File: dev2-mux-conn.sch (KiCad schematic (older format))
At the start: 8 parts, among them J28 Device 2, U11 MAX4533, U14 74LS32, U36 LTC1391, U37 LTC1391, U38 LTC1391, U7 TS12A44514

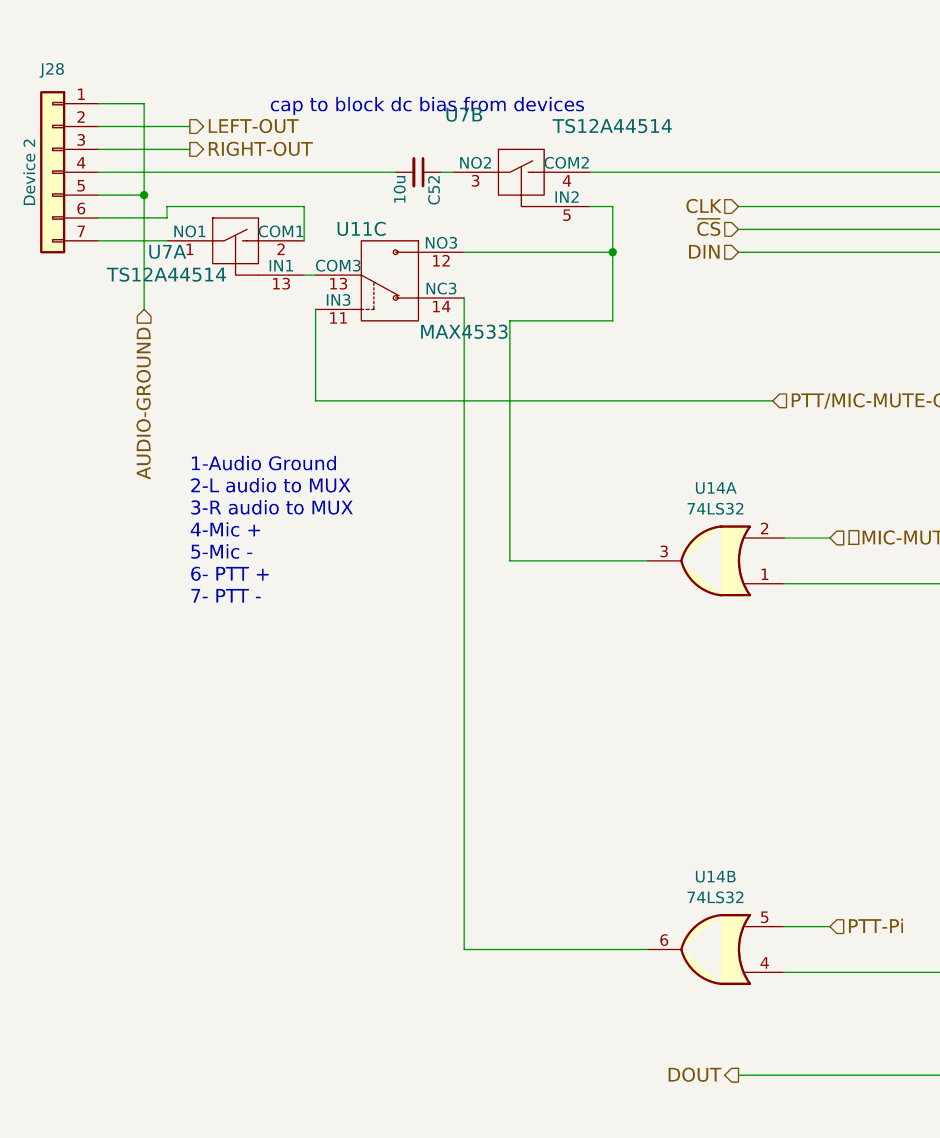
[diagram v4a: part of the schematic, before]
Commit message: Re arranging pins and component names
to make pcb layout saner
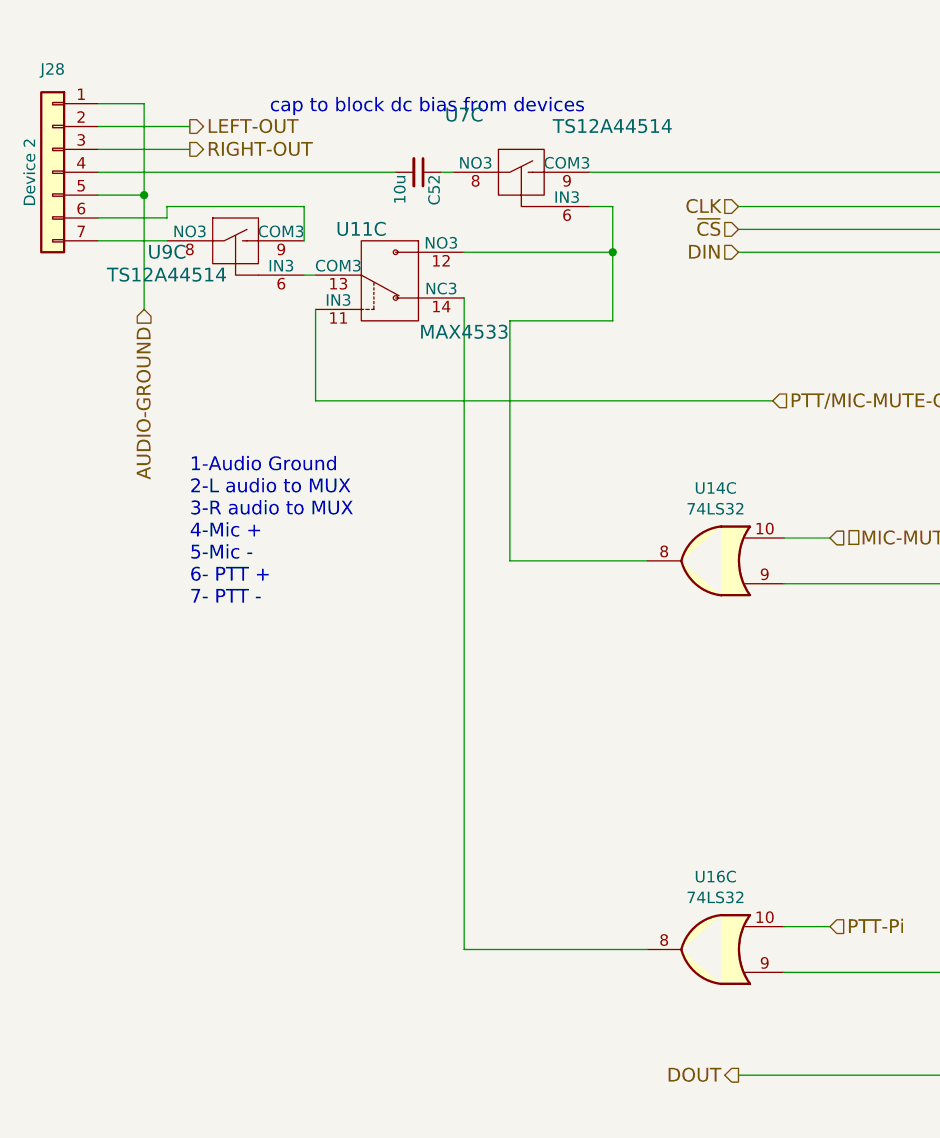
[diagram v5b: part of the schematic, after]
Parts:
- U14: Pricing (none) -> 0.00@0
- U16: renamed from U14; Pricing (none) -> 0.00@0
- renumbered U7 to U9
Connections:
- net MIC-MUTE-Pi: now also U14.10; no longer U14.2
- net PTT-Pi: now also U16.10; no longer U16.5
- net at J28.6 (Pin_6): now also U9.9 (COM3); no longer U9.2 (COM1)
- net at J28.7 (Pin_7): now also U9.8 (NO3); no longer U9.1 (NO1)
- net at C52.1: now also U7.8 (NO3); no longer U7.3 (NO2)
- net at U36.15 (D): now also U7.9 (COM3); no longer U7.4 (COM2)
- net at U11.13 (COM3): now also U9.6 (IN3); no longer U9.13 (IN1)
- net at U11.14 (NC3): now also U16.8; no longer U16.6
- net at U37.15 (D): now also U14.9; no longer U14.1
- net at U38.15 (D): now also U16.9; no longer U16.4
- new net: U11.12 (NO3), U14.8, U7.6 (IN3)
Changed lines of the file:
@@
 $Comp
 L TS12A44514 U?
-U 2 1 58EAA0E5
+U 3 1 58EAA0E5
 P 2950 1150
 AR Path="/58DEDA38/58EAA0E5" Ref="U?"  Part="1"
 AR Path="/58DEDA38/58E9E25B/58EAA0E5" Ref="U?"  Part="1"
-AR Path="/58DEDA38/58E9E991/58EAA0E5" Ref="U7"  Part="2"
+AR Path="/58DEDA38/58E9E991/58EAA0E5" Ref="U7"  Part="3"
 F 0 "U7" H 2700 1400 60  0000 C CNN
 F 1 "TS12A44514" H 3350 1350 60  0000 C CNN
@@
 F 7 "TSSOP14" H 3250 2350 60  0001 C CNN "Package ID"
 F 8 "0.00@0" H 3000 2150 60  0001 C CNN "Pricing"
-	2    2950 1150
+	3    2950 1150
 	1    0    0    -1
 $EndComp
 $Comp
 L TS12A44514 U?
-U 1 1 58EAA0F1
+U 3 1 58EAA0F1
 P 1700 1450
 AR Path="/58DEDA38/58EAA0F1" Ref="U?"  Part="1"
 AR Path="/58DEDA38/58E9E25B/58EAA0F1" Ref="U?"  Part="1"
-AR Path="/58DEDA38/58E9E991/58EAA0F1" Ref="U7"  Part="1"
-F 0 "U7" H 1400 1400 60  0000 C CNN
+AR Path="/58DEDA38/58E9E991/58EAA0F1" Ref="U9"  Part="3"
+F 0 "U9" H 1400 1400 60  0000 C CNN
 F 1 "TS12A44514" H 1400 1300 60  0000 C CNN
 F 2 "Housings_SSOP:TSSOP-14_4.4x5mm_Pitch0.65mm" H 2200 2750 60  0001 C CNN
@@
 F 7 "TSSOP14" H 2000 2650 60  0001 C CNN "Package ID"
 F 8 "0.00@0" H 1750 2450 60  0001 C CNN "Pricing"
-	1    1700 1450
+	3    1700 1450
 	1    0    0    -1
 $EndComp
@@
 $Comp
 L 74LS32 U?
-U 1 1 59D24FEE
+U 3 1 59D24FEE
 P 3800 2850
 AR Path="/58DEDA38/58E9E2BE/59D24FEE" Ref="U?"  Part="1"
-AR Path="/58DEDA38/58E9E991/59D24FEE" Ref="U14"  Part="1"
+AR Path="/58DEDA38/58E9E991/59D24FEE" Ref="U14"  Part="3"
 F 0 "U14" H 3800 2533 50  0000 C CNN
 F 1 "74LS32" H 3800 2624 50  0000 C CNN
 F 2 "Housings_SSOP:SSOP-14_5.3x6.2mm_Pitch0.65mm" H 3800 2850 50  0001 C CNN
 F 3 "" H 3800 2850 50  0001 C CNN
-	1    3800 2850
+F 4 "0.00@0" H 3800 2850 60  0001 C CNN "Pricing"
+	3    3800 2850
 	-1   0    0    1
 $EndComp
@@
 $Comp
 L 74LS32 U?
-U 2 1 59D24FF6
+U 3 1 59D24FF6
 P 3800 4550
 AR Path="/58DEDA38/58E9E2BE/59D24FF6" Ref="U?"  Part="2"
 AR Path="/58DEDA38/58E9E9F4/59D24FF6" Ref="U?"  Part="2"
-AR Path="/58DEDA38/58E9E991/59D24FF6" Ref="U14"  Part="2"
-F 0 "U14" H 3800 4233 50  0000 C CNN
+AR Path="/58DEDA38/58E9E991/59D24FF6" Ref="U16"  Part="3"
+F 0 "U16" H 3800 4233 50  0000 C CNN
 F 1 "74LS32" H 3800 4324 50  0000 C CNN
 F 2 "Housings_SSOP:SSOP-14_5.3x6.2mm_Pitch0.65mm" H 3800 4550 50  0001 C CNN
 F 3 "" H 3800 4550 50  0001 C CNN
-	2    3800 4550
+F 4 "0.00@0" H 3800 4550 60  0001 C CNN "Pricing"
+	3    3800 4550
 	-1   0    0    1
 $EndComp

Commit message: Adding libraries and Notes
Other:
- note added: "Device power provided by\nexternal connection"
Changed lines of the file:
@@
 LIBS:interface
 LIBS:SW-gElectroMech
+LIBS:SW-Analog
+LIBS:SW-Semtech
 LIBS:edc-mux-board-cache
 EELAYER 26 0
@@
 $Descr USLetter 11000 8500
 encoding utf-8
-Sheet 7 14
+Sheet 6 14
 Title ""
 Date ""
@@
 	1    0    0    -1
 $EndComp
+Text Notes -650 1150 0    60   ~ 0
+Device power provided by\nexternal connection
 $EndSCHEMATC
